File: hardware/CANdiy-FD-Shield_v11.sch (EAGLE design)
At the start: 59 parts, among them IC1 MCP2517FDT-H/SL, IC3 MCP2562FDT-E/SN, Q1 16MHz, U1 UNO_ISP, X1 PASSER-07, X2 PASSER-07, X3 PASSER-07

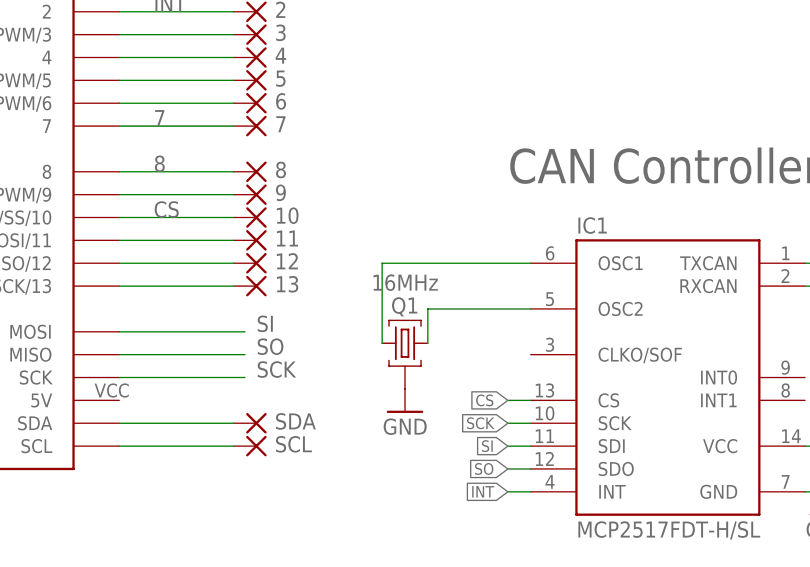
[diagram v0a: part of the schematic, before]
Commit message: updated schematics
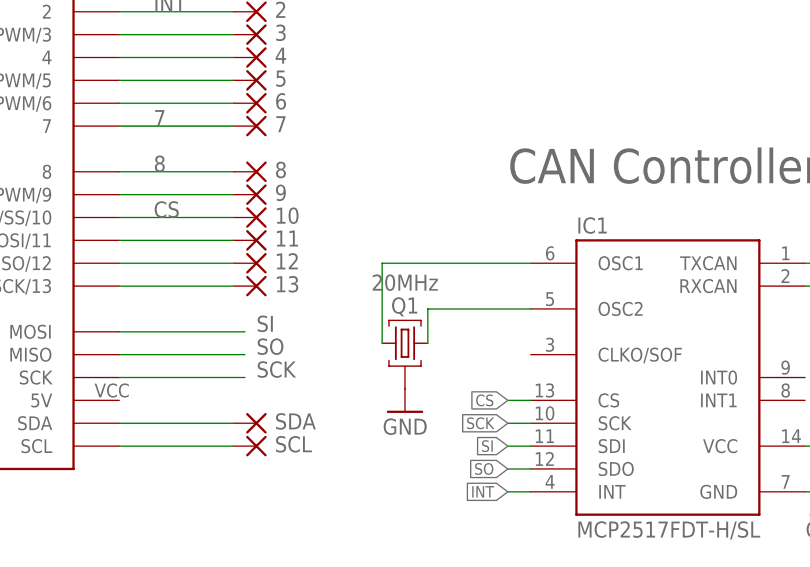
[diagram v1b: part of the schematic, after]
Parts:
- Q1: value 16MHz -> 20MHz
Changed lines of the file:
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@@
 <setting verticaltext="up"/>
 </settings>
-<grid distance="0.05" unitdist="inch" unit="inch" style="lines" multiple="1" display="yes" altdistance="0.01" altunitdist="inch" altunit="inch"/>
+<grid distance="0.1" unitdist="inch" unit="inch" style="lines" multiple="1" display="no" altdistance="0.01" altunitdist="inch" altunit="inch"/>
 <layers>
-<layer number="1" name="Top" color="4" fill="1" visible="yes" active="no"/>
-<layer number="2" name="Route2" color="1" fill="3" visible="yes" active="no"/>
-<layer number="3" name="Route3" color="4" fill="3" visible="yes" active="no"/>
-<layer number="4" name="Route4" color="1" fill="4" visible="yes" active="no"/>
-<layer number="5" name="Route5" color="4" fill="4" visible="yes" active="no"/>
-<layer number="6" name="Route6" color="1" fill="8" visible="yes" active="no"/>
-<layer number="7" name="Route7" color="4" fill="8" visible="yes" active="no"/>
-<layer number="8" name="Route8" color="1" fill="2" visible="yes" active="no"/>
-<layer number="9" name="Route9" color="4" fill="2" visible="yes" active="no"/>
-<layer number="10" name="Route10" color="1" fill="7" visible="yes" active="no"/>
-<layer number="11" name="Route11" color="4" fill="7" visible="yes" active="no"/>
-<layer number="12" name="Route12" color="1" fill="5" visible="yes" active="no"/>
-<layer number="13" name="Route13" color="4" fill="5" visible="yes" active="no"/>
-<layer number="14" name="Route14" color="1" fill="6" visible="yes" active="no"/>
-<layer number="15" name="Route15" color="4" fill="6" visible="yes" active="no"/>
-<layer number="16" name="Bottom" color="1" fill="1" visible="yes" active="no"/>
-<layer number="17" name="Pads" color="2" fill="1" visible="yes" active="no"/>
-<layer number="18" name="Vias" color="2" fill="1" visible="yes" active="no"/>
-<layer number="19" name="Unrouted" color="6" fill="1" visible="yes" active="no"/>
-<layer number="20" name="Dimension" color="15" fill="1" visible="yes" active="no"/>
-<layer number="21" name="tPlace" color="7" fill="1" visible="yes" active="no"/>
-<layer number="22" name="bPlace" color="7" fill="1" visible="yes" active="no"/>
-<layer number="23" name="tOrigins" color="15" fill="1" visible="yes" active="no"/>
-<layer number="24" name="bOrigins" color="15" fill="1" visible="yes" active="no"/>
-<layer number="25" name="tNames" color="7" fill="1" visible="yes" active="no"/>
-<layer number="26" name="bNames" color="7" fill="1" visible="yes" active="no"/>
-<layer number="27" name="tValues" color="7" fill="1" visible="yes" active="no"/>
-<layer number="28" name="bValues" color="7" fill="1" visible="yes" active="no"/>
+<layer number="1" name="Top" color="4" fill="1" visible="no" active="no"/>
+<layer number="2" name="Route2" color="1" fill="3" visible="no" active="no"/>
+<layer number="3" name="Route3" color="4" fill="3" visible="no" active="no"/>
+<layer number="4" name="Route4" color="1" fill="4" visible="no" active="no"/>
+<layer number="5" name="Route5" color="4" fill="4" visible="no" active="no"/>
+<layer number="6" name="Route6" color="1" fill="8" visible="no" active="no"/>
+<layer number="7" name="Route7" color="4" fill="8" visible="no" active="no"/>
+<layer number="8" name="Route8" color="1" fill="2" visible="no" active="no"/>
+<layer number="9" name="Route9" color="4" fill="2" visible="no" active="no"/>
+<layer number="10" name="Route10" color="1" fill="7" visible="no" active="no"/>
+<layer number="11" name="Route11" color="4" fill="7" visible="no" active="no"/>
+<layer number="12" name="Route12" color="1" fill="5" visible="no" active="no"/>
+<layer number="13" name="Route13" color="4" fill="5" visible="no" active="no"/>
+<layer number="14" name="Route14" color="1" fill="6" visible="no" active="no"/>
+<layer number="15" name="Route15" color="4" fill="6" visible="no" active="no"/>
+<layer number="16" name="Bottom" color="1" fill="1" visible="no" active="no"/>
+<layer number="17" name="Pads" color="2" fill="1" visible="no" active="no"/>
+<layer number="18" name="Vias" color="2" fill="1" visible="no" active="no"/>
+<layer number="19" name="Unrouted" color="6" fill="1" visible="no" active="no"/>
+<layer number="20" name="Dimension" color="15" fill="1" visible="no" active="no"/>
+<layer number="21" name="tPlace" color="7" fill="1" visible="no" active="no"/>
+<layer number="22" name="bPlace" color="7" fill="1" visible="no" active="no"/>
+<layer number="23" name="tOrigins" color="15" fill="1" visible="no" active="no"/>
+<layer number="24" name="bOrigins" color="15" fill="1" visible="no" active="no"/>
+<layer number="25" name="tNames" color="7" fill="1" visible="no" active="no"/>
+<layer number="26" name="bNames" color="7" fill="1" visible="no" active="no"/>
+<layer number="27" name="tValues" color="7" fill="1" visible="no" active="no"/>
+<layer number="28" name="bValues" color="7" fill="1" visible="no" active="no"/>
 <layer number="29" name="tStop" color="7" fill="3" visible="no" active="no"/>
 <layer number="30" name="bStop" color="7" fill="6" visible="no" active="no"/>
@@
 <layer number="35" name="tGlue" color="7" fill="4" visible="no" active="no"/>
 <layer number="36" name="bGlue" color="7" fill="5" visible="no" active="no"/>
-<layer number="37" name="tTest" color="7" fill="1" visible="yes" active="no"/>
-<layer number="38" name="bTest" color="7" fill="1" visible="yes" active="no"/>
+<layer number="37" name="tTest" color="7" fill="1" visible="no" active="no"/>
+<layer number="38" name="bTest" color="7" fill="1" visible="no" active="no"/>
 <layer number="39" name="tKeepout" color="4" fill="11" visible="no" active="no"/>
 <layer number="40" name="bKeepout" color="1" fill="11" visible="no" active="no"/>
@@
 <layer number="44" name="Drills" color="7" fill="1" visible="no" active="no"/>
 <layer number="45" name="Holes" color="7" fill="1" visible="no" active="no"/>
-<layer number="46" name="Milling" color="3" fill="1" visible="yes" active="no"/>
-<layer number="47" name="Measures" color="7" fill="1" visible="yes" active="no"/>
-<layer number="48" name="Document" color="7" fill="1" visible="yes" active="no"/>
-<layer number="49" name="Reference" color="7" fill="1" visible="yes" active="no"/>
-<layer number="50" name="dxf" color="7" fill="1" visible="yes" active="no"/>
-<layer number="51" name="tDocu" color="7" fill="1" visible="yes" active="no"/>
-<layer number="52" name="bDocu" color="7" fill="1" visible="yes" active="no"/>
+<layer number="46" name="Milling" color="3" fill="1" visible="no" active="no"/>
+<layer number="47" name="Measures" color="7" fill="1" visible="no" active="no"/>
+<layer number="48" name="Document" color="7" fill="1" visible="no" active="no"/>
+<layer number="49" name="Reference" color="7" fill="1" visible="no" active="no"/>
+<layer number="50" name="dxf" color="7" fill="1" visible="no" active="no"/>
+<layer number="51" name="tDocu" color="7" fill="1" visible="no" active="no"/>
+<layer number="52" name="bDocu" color="7" fill="1" visible="no" active="no"/>
 <layer number="90" name="Modules" color="5" fill="1" visible="yes" active="yes"/>
 <layer number="91" name="Nets" color="2" fill="1" visible="yes" active="yes"/>
@@
 <part name="GND8" library="supply1" deviceset="GND" device=""/>
 <part name="IC1" library="we-chip" deviceset="MCP2517FD" device="T-H/SL"/>
-<part name="Q1" library="we-rcl" deviceset="CRYSTAL-RES" device="-32" value="16MHz"/>
+<part name="Q1" library="we-rcl" deviceset="CRYSTAL-RES" device="-32" value="20MHz"/>
 <part name="D1" library="we-rcl" deviceset="D_SCHOTTKY" device="-SOD323"/>
 </parts>
